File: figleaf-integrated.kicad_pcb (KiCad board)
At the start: 2 copper layers, 145 x 105 mm, 62 parts, among them J2 HRO_TYPE-C-31-M-14, J3 Battery, J9 TC2030_SWD, Q2 2N7002, SW1 PWR, SW2 RST, U1 SRV05-4, U10 MAX17048, U3 BQ24075, U8 nRF52840_moko_mk08

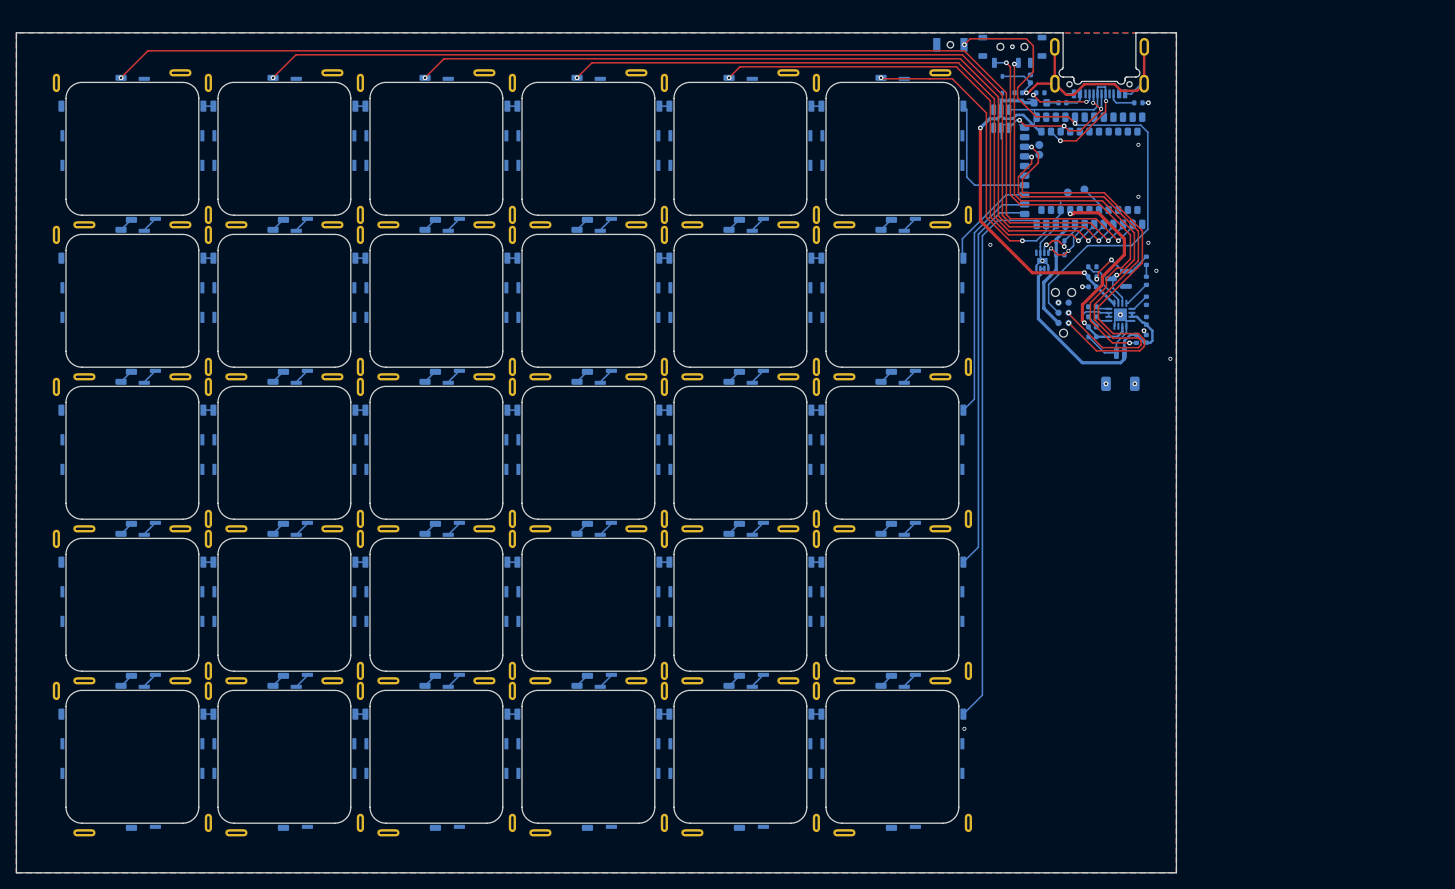
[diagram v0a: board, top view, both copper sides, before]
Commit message: move usb outwards + add mounting holes + fillet
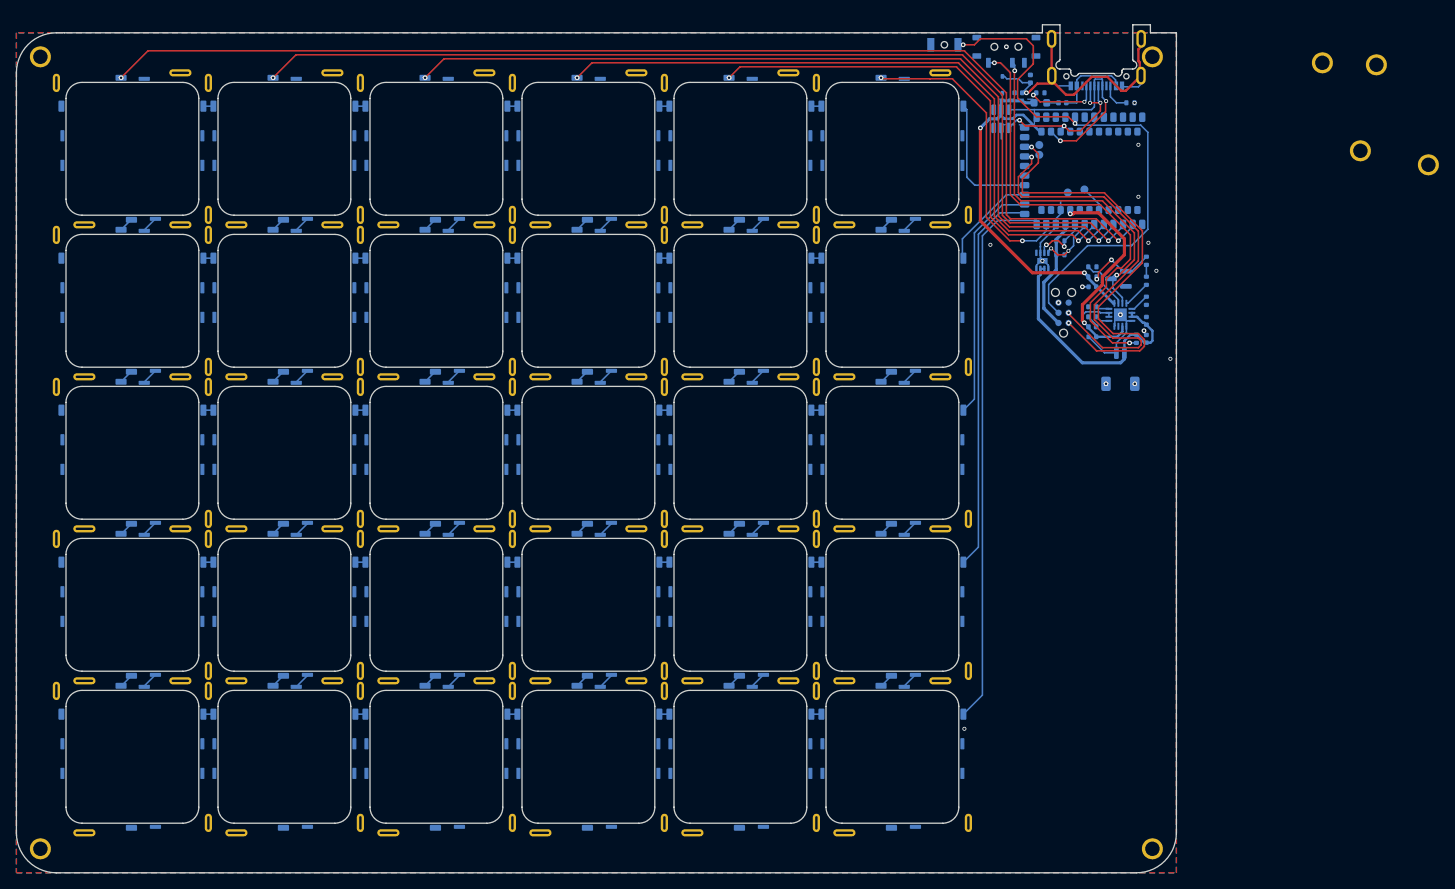
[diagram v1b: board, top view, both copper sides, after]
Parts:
- added H1: MountingHole, Graz_Footprints:m1.6, F.Cu at (15.5, 15.5)
- added H2: MountingHole, Graz_Footprints:m1.6, F.Cu at (15.5, 114.5)
- added H3: MountingHole, Graz_Footprints:m1.6, F.Cu at (154.5, 114.5)
- added H4: MountingHole, Graz_Footprints:m1.6, F.Cu at (154.5, 15.5)
- added H5: MountingHole, Graz_Footprints:m1.6, F.Cu at (180.5, 27.2)
- added H6: MountingHole, Graz_Footprints:m1.6, F.Cu at (189.0, 29.0)
- added H7: MountingHole, Graz_Footprints:m1.6, F.Cu at (175.8, 16.2)
- added H8: MountingHole, Graz_Footprints:m1.6, F.Cu at (182.5, 16.5)
- moved J2 1.07 mm to (147.5, 17.9)
- moved R1 0.99 mm to (151.8, 21.2)
- moved SW1 0.75 mm to (136.2, 14.2)
- moved SW2 0.75 mm to (128.5, 14.0)
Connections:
- SW1 pad MP: GND_L -> (no net)
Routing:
- net Earth: track 37.8 -> 41.4 mm
- net USB-D-: track 18.9 -> 21.0 mm
- net USB-D+: track 26.8 -> 28.4 mm
- net VBUS: track 9.23 -> 10.1 mm
- net RST: track 66.9 -> 67.7 mm
- net GND_L: track 32.1 -> 31.3 mm
- net Net-(J2-CC1): track 8.75 -> 9.33 mm
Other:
- board size 145 x 105 mm -> 145 x 106 mm

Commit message: progress
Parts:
- moved F1 1.60 mm to (138.9, 21.2)
- moved J2 1.60 mm to (145.9, 17.9)
- moved L1 1.60 mm to (141.7, 21.2)
- moved R1 1.60 mm to (150.2, 21.2)
- moved R2 1.60 mm to (138.9, 20.0), turned to 0 degrees
- moved C1 1.25 mm to (136.5, 20.0)
- moved D1 1.25 mm to (134.5, 19.0)
- moved SW1 1.00 mm to (135.2, 14.2)
- moved L2 0.50 mm to (138.8, 18.2)
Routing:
- net GND_L: track 31.3 -> 34.9 mm
- net Earth: track 41.4 -> 38.3 mm, vias 1 -> 0
- net USB-D+: track 28.4 -> 25.9 mm
- net Net-(J2-CC1): track 9.33 -> 7.71 mm
- net +5V: track 48.7 -> 47.1 mm
- net USB-D-: track 21.0 -> 19.9 mm
- net Net-(F1-Pad1): track 1.48 -> 0.47 mm
- net VBUS: track 10.1 -> 9.30 mm
- net Net-(SW1-A): track 55.6 -> 56.2 mm

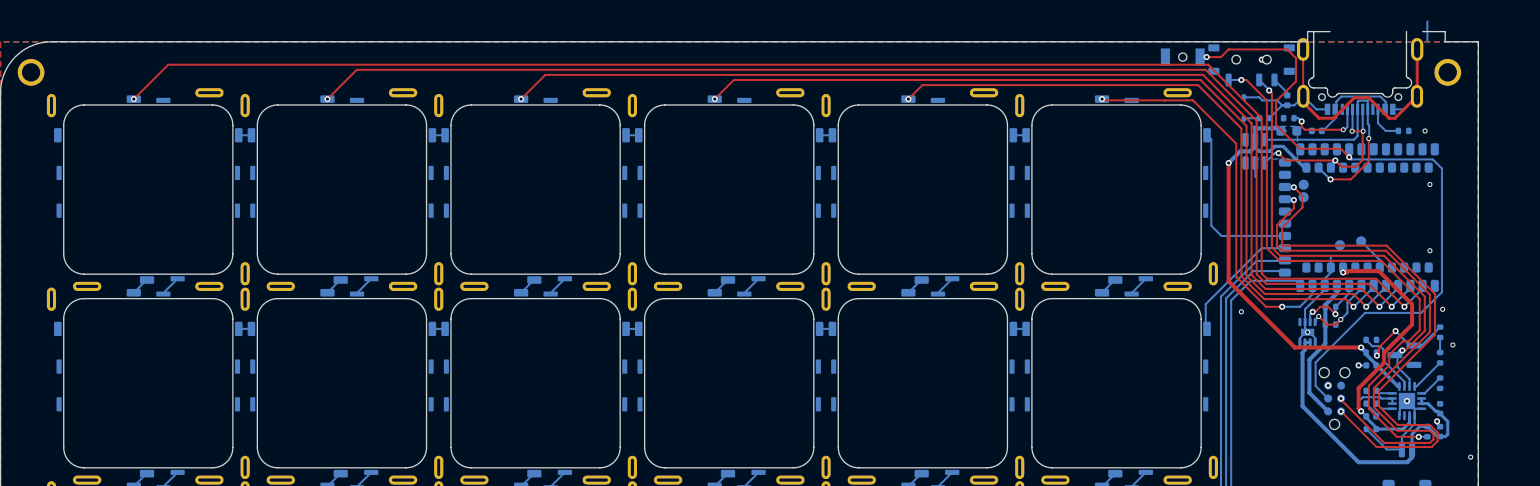
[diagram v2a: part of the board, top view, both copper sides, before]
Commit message: progress on mounting hole + moving usb
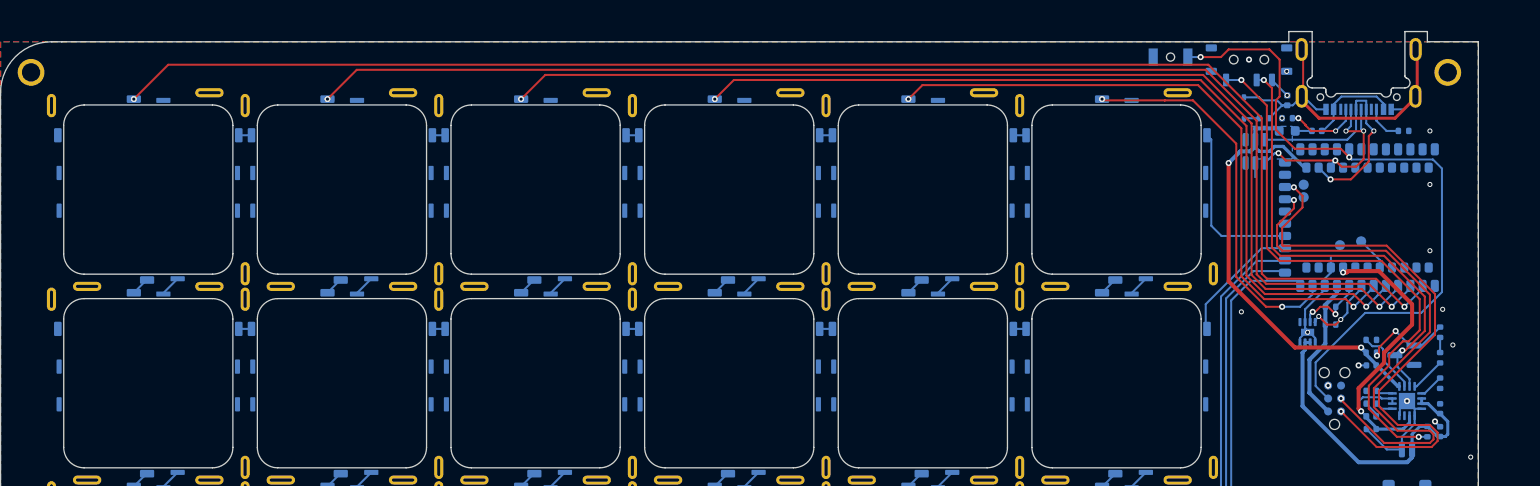
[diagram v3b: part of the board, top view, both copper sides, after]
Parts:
- moved SW2 1.20 mm to (127.3, 14.0)
- moved SW1 0.25 mm to (135.0, 14.2)
- moved F1 0.16 mm to (138.8, 21.2)
- moved R2 0.16 mm to (138.8, 20.0)
- moved J2 0.15 mm to (145.8, 17.9)
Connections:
- SW1 pad MP: (no net) -> GND_L
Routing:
- net Net-(F1-Pad1): track 0.47 -> 2.11 mm
- net USB-D-: track 19.9 -> 20.9 mm
- net RST: track 67.7 -> 66.8 mm
- net +5V: track 47.1 -> 46.6 mm
- net GND_L: track 34.9 -> 35.1 mm, vias 16 -> 19
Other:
- outline, holes or cut-outs redrawn

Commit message: DRC fixws
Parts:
- moved C1 4.14 mm to (132.8, 18.2), turned to -90 degrees
- moved L1 0.85 mm to (142.5, 21.2)
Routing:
- net GND_L: track 35.1 -> 31.4 mm
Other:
- outline, holes or cut-outs redrawn

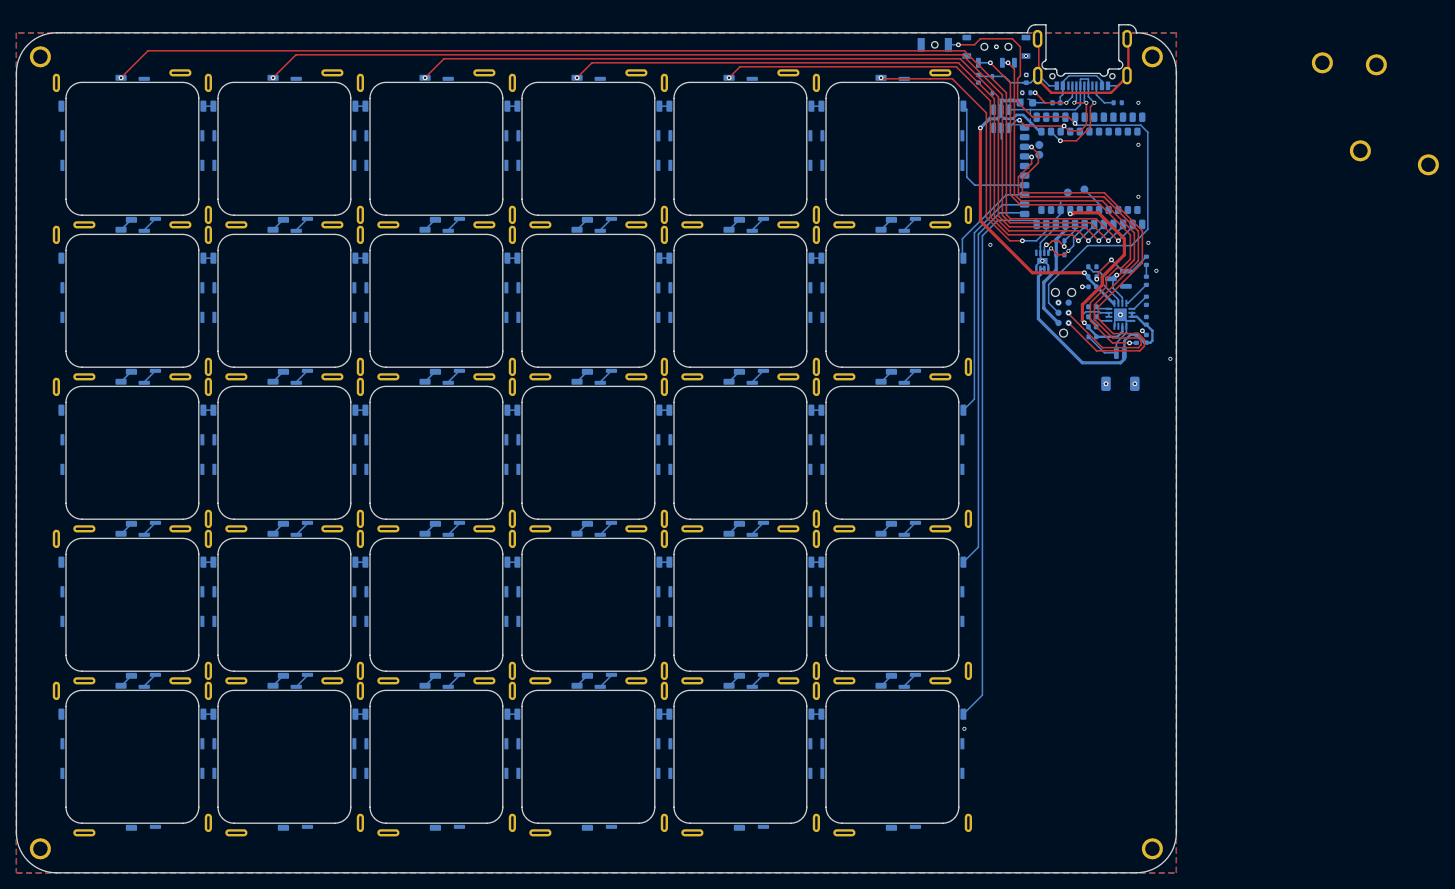
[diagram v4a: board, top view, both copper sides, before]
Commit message: move silkscreen
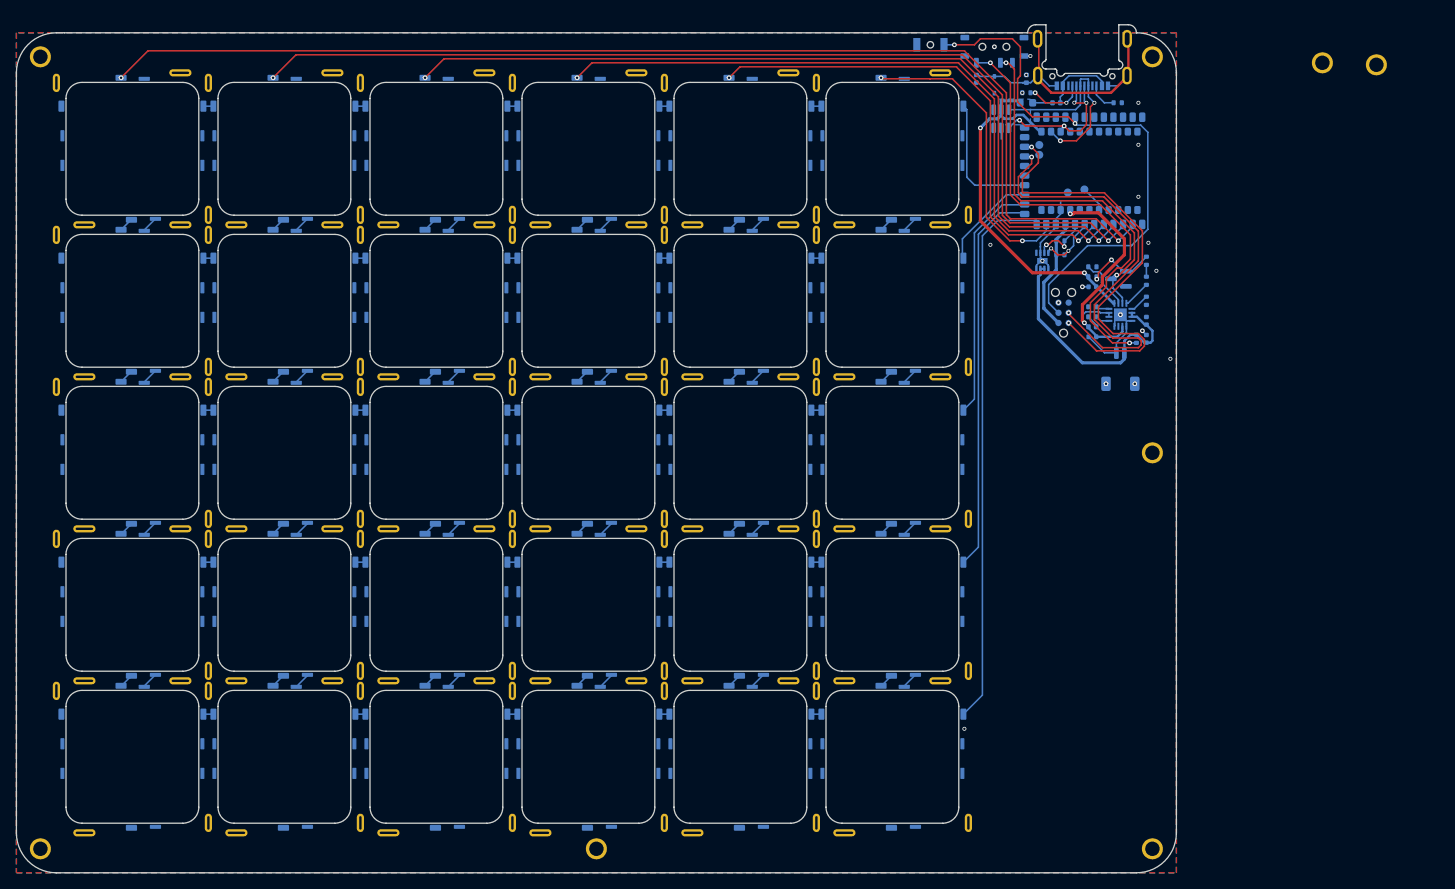
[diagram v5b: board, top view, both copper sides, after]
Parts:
- moved H5 129.4 mm to (85.0, 114.5)
- moved H6 56.1 mm to (154.5, 73.2)
- moved SW2 0.55 mm to (126.8, 14.0)
- moved C1 0.25 mm to (132.5, 18.2)
- moved D1 0.25 mm to (134.8, 19.0)
- moved SW1 0.25 mm to (134.8, 14.2)
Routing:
- net GND_L: track 31.4 -> 32.2 mm
- net Net-(F1-Pad1): track 2.11 -> 2.83 mm
- net RST: track 66.8 -> 67.4 mm

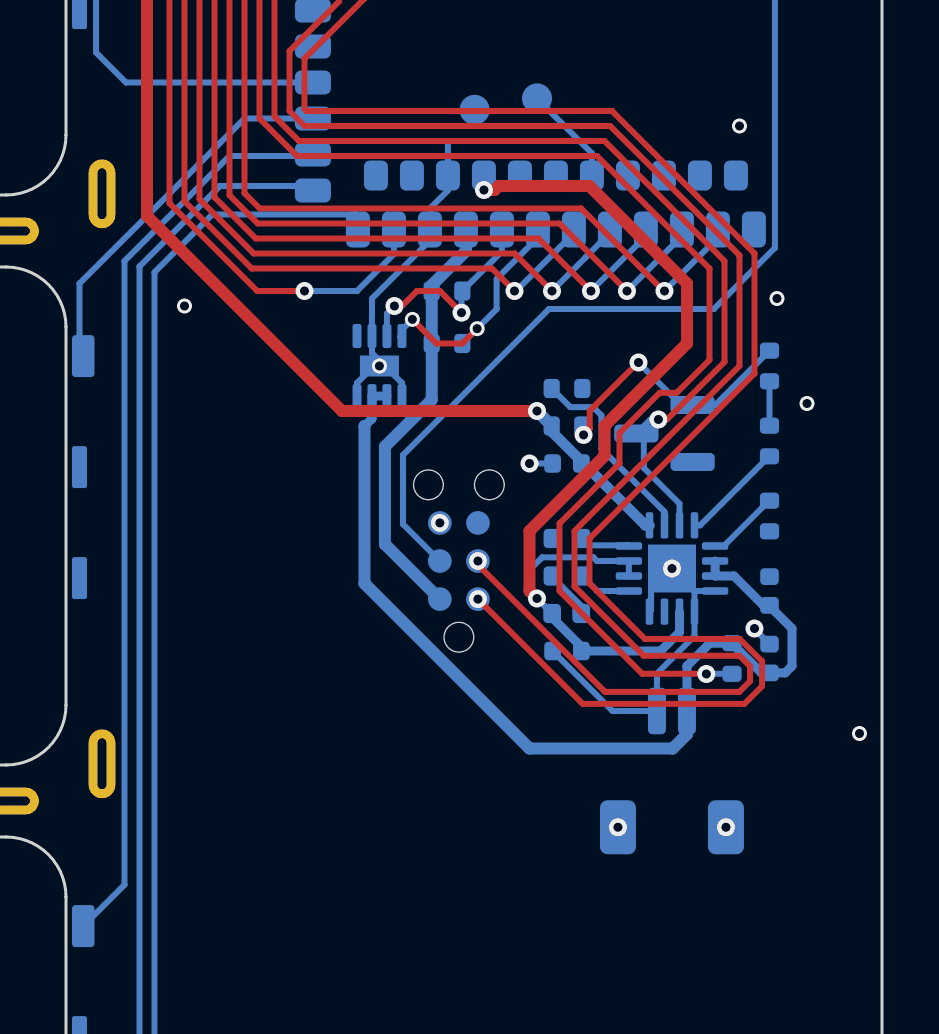
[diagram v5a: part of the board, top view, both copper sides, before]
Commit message: find device center
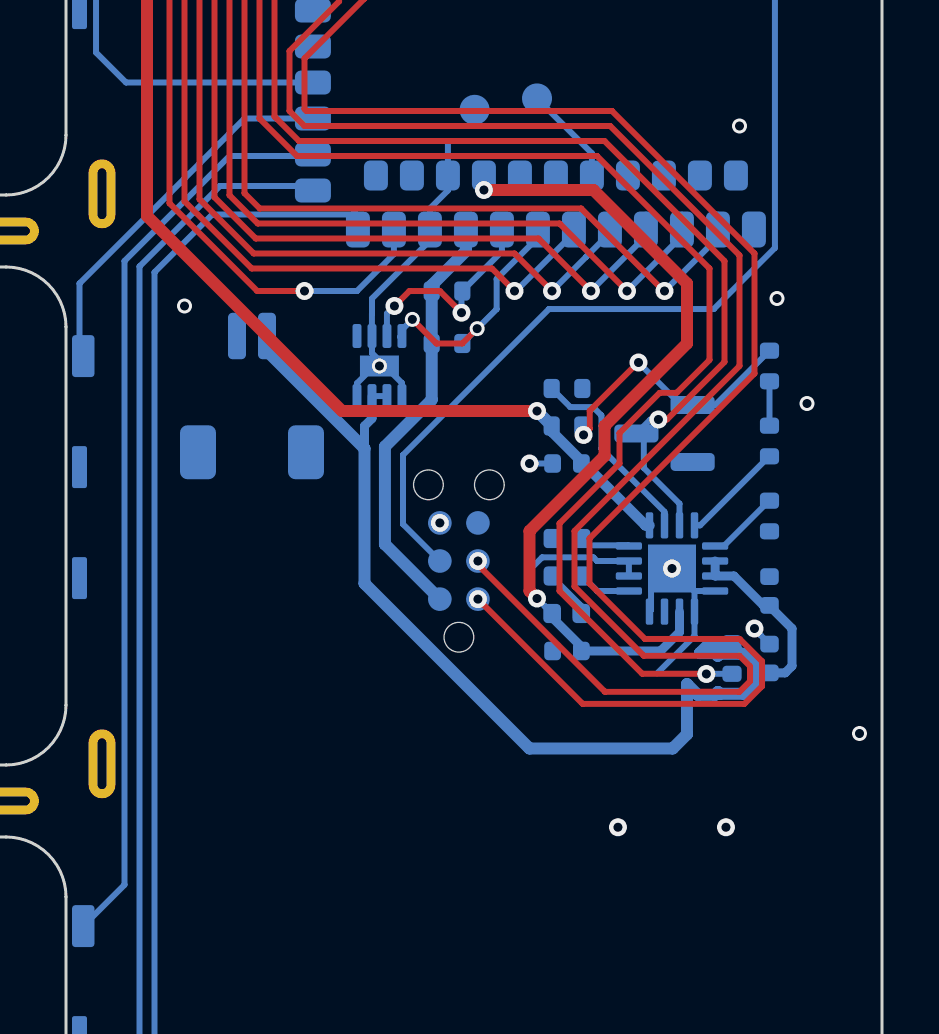
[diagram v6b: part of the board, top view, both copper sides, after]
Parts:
- moved J3 18.8 mm to (136.5, 42.0)
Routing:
- net +BATT: track 31.7 -> 40.8 mm
- net GND_L: track 32.2 -> 26.6 mm
